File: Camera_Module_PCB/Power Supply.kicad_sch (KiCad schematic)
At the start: 18 parts

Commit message: Made some small additions and notes
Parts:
- gave numbers to parts that had none: 13
- renumbered C1 to C5, TypeCinput to J4, PMIC to U2
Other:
- note added: "To differentiate VDDA and VDD, we can remove the inductor here and slot the inductor in the capacitor array that is present in the main schematic page"
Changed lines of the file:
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@@
 		)
 	)
+	(text "To differentiate VDDA and VDD,\nwe can remove the inductor \nhere and slot the inductor \nin the capacitor array that \nis present in the main \nschematic page\n"
+		(exclude_from_sim no)
+		(at 72.39 142.748 0)
+		(effects
+			(font
+				(size 1.27 1.27)
+			)
+		)
+	)
 	(text "Type C Connector "
 		(exclude_from_sim no)
@@
 		(dnp no)
 		(fields_autoplaced yes)
-		(property "Reference" "D?"
+		(property "Reference" "D4"
 			(at 157.48 77.1524 90)
 			(effects
@@
 		(on_board yes)
 		(dnp no)
-		(property "Reference" "C?"
+		(property "Reference" "C6"
 			(at 267.97 43.1862 0)
 			(effects
@@
 		(dnp no)
 		(fields_autoplaced yes)
-		(property "Reference" "#PWR?"
+		(property "Reference" "#PWR06"
 			(at 97.79 73.66 0)
 			(effects
@@
 		(dnp no)
 		(fields_autoplaced yes)
-		(property "Reference" "#PWR?"
+		(property "Reference" "#PWR04"
 			(at 35.56 24.13 0)
 			(effects
@@
 		(dnp no)
 		(fields_autoplaced yes)
-		(property "Reference" "#PWR?"
+		(property "Reference" "#PWR013"
 			(at 154.94 53.34 0)
 			(effects
@@
 		(dnp no)
 		(fields_autoplaced yes)
-		(property "Reference" "#PWR?"
+		(property "Reference" "#PWR05"
 			(at 85.09 24.13 0)
 			(effects
@@
 		(dnp no)
 		(fields_autoplaced yes)
-		(property "Reference" "#PWR?"
+		(property "Reference" "#PWR017"
 			(at 246.38 95.25 0)
 			(effects
@@
 		(dnp no)
 		(fields_autoplaced yes)
-		(property "Reference" "R?"
+		(property "Reference" "R3"
 			(at 139.7 68.5799 0)
 			(effects
@@
 		(dnp no)
 		(fields_autoplaced yes)
-		(property "Reference" "U?"
+		(property "Reference" "U3"
 			(at 62.23 114.3 0)
 			(effects
@@
 		(dnp no)
 		(fields_autoplaced yes)
-		(property "Reference" "#PWR?"
+		(property "Reference" "#PWR09"
 			(at 100.33 46.99 0)
 			(effects
@@
 		(dnp no)
 		(fields_autoplaced yes)
-		(property "Reference" "TypeCinput"
+		(property "Reference" "J4"
 			(at 60.96 25.4 0)
 			(effects
@@
 		(dnp no)
 		(fields_autoplaced yes)
-		(property "Reference" "R?"
+		(property "Reference" "R4"
 			(at 148.59 68.5799 0)
 			(effects
@@
 		(dnp no)
 		(fields_autoplaced yes)
-		(property "Reference" "PMIC"
+		(property "Reference" "U2"
 			(at 209.55 38.1 0)
 			(effects
@@
 		(dnp no)
 		(fields_autoplaced yes)
-		(property "Reference" "C?"
+		(property "Reference" "C1"
 			(at 123.19 129.5462 0)
 			(effects
@@
 		(dnp no)
 		(fields_autoplaced yes)
-		(property "Reference" "SW?"
+		(property "Reference" "SW2"
 			(at 260.35 81.28 0)
 			(effects
@@
 		(dnp no)
 		(fields_autoplaced yes)
-		(property "Reference" "D?"
+		(property "Reference" "D2"
 			(at 139.7 77.1524 90)
 			(effects
@@
 		(dnp no)
 		(fields_autoplaced yes)
-		(property "Reference" "R?"
+		(property "Reference" "R6"
 			(at 271.78 80.0099 0)
 			(effects
@@
 		(dnp no)
 		(fields_autoplaced yes)
-		(property "Reference" "#PWR?"
+		(property "Reference" "#PWR016"
 			(at 273.05 43.18 0)
 			(effects
@@
 		(dnp no)
 		(fields_autoplaced yes)
-		(property "Reference" "#PWR?"
+		(property "Reference" "#PWR012"
 			(at 119.38 127 0)
 			(effects
@@
 		(dnp no)
 		(fields_autoplaced yes)
-		(property "Reference" "R?"
+		(property "Reference" "R5"
 			(at 157.48 68.5799 0)
 			(effects
@@
 		(on_board yes)
 		(dnp no)
-		(property "Reference" "#PWR?"
+		(property "Reference" "#PWR015"
 			(at 265.43 53.34 0)
 			(effects
@@
 		(dnp no)
 		(fields_autoplaced yes)
-		(property "Reference" "C1"
+		(property "Reference" "C5"
 			(at 102.87 36.8362 0)
 			(effects
@@
 		(on_board yes)
 		(dnp no)
-		(property "Reference" "L?"
+		(property "Reference" "L1"
 			(at 102.87 128.27 0)
 			(effects
@@
 		(dnp no)
 		(fields_autoplaced yes)
-		(property "Reference" "#PWR?"
+		(property "Reference" "#PWR01"
 			(at 120.65 146.05 0)
 			(effects
@@
 		(dnp no)
 		(fields_autoplaced yes)
-		(property "Reference" "#PWR?"
+		(property "Reference" "#PWR08"
 			(at 22.86 52.07 0)
 			(effects
@@
 		(dnp no)
 		(fields_autoplaced yes)
-		(property "Reference" "#PWR?"
+		(property "Reference" "#PWR011"
 			(at 135.89 124.46 0)
 			(effects
@@
 		(dnp no)
 		(fields_autoplaced yes)
-		(property "Reference" "#PWR?"
+		(property "Reference" "#PWR03"
 			(at 25.4 132.08 0)
 			(effects
@@
 		(dnp no)
 		(fields_autoplaced yes)
-		(property "Reference" "#PWR?"
+		(property "Reference" "#PWR07"
 			(at 35.56 71.12 0)
 			(effects
@@
 		(dnp no)
 		(fields_autoplaced yes)
-		(property "Reference" "#PWR?"
+		(property "Reference" "#PWR02"
 			(at 101.6 104.14 0)
 			(effects
@@
 		(dnp no)
 		(fields_autoplaced yes)
-		(property "Reference" "D?"
+		(property "Reference" "D3"
 			(at 148.59 77.1524 90)
 			(effects
@@
 		(dnp no)
 		(fields_autoplaced yes)
-		(property "Reference" "C?"
+		(property "Reference" "C2"
 			(at 104.14 115.5635 0)
 			(effects

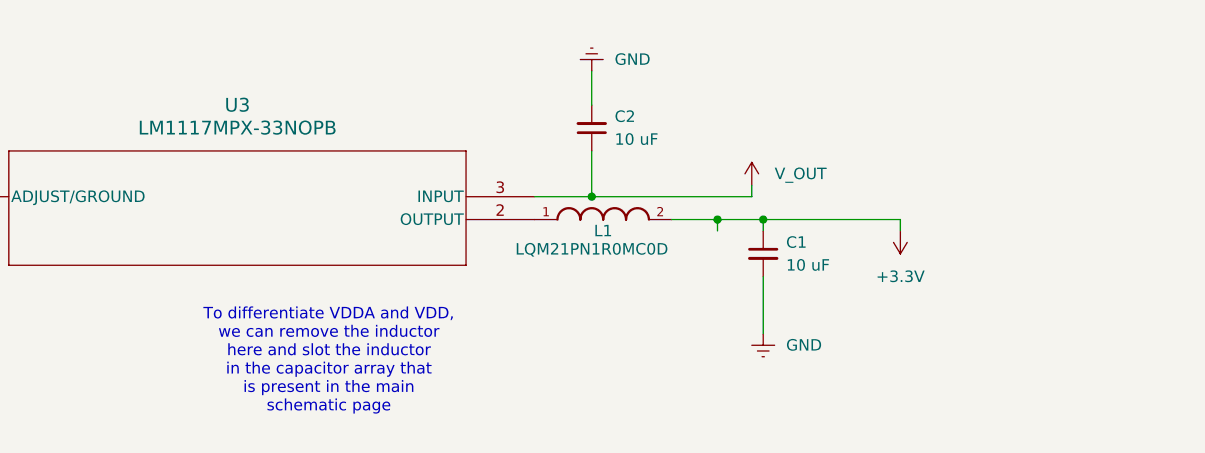
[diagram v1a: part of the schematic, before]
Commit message: Added components and began connections
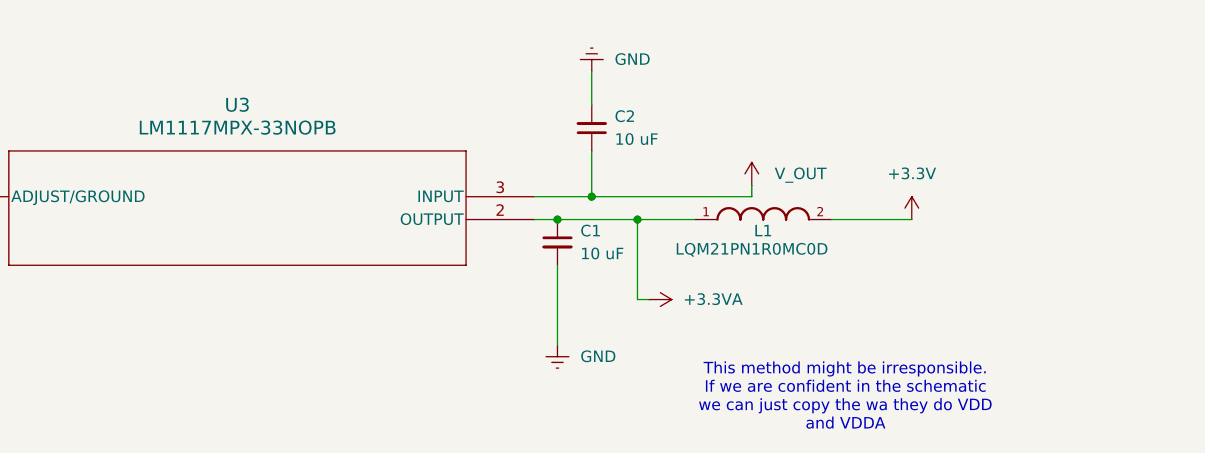
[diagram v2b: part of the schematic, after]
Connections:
- net +3.3V: no longer C1.1
- net +3.3VA: now reaches L1.1, U3.2 (OUTPUT)
- net +3.3VA: now also C1.1
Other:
- note added: "This method might be irresponsible. If we are confident in the schematic we can just copy the wa they do VDD and VDDA"
- note removed: "To differentiate VDDA and VDD, we can remove the inductor here and slot the inductor in the capacitor array that is present in the main schematic page"
- moved on the sheet: C1, L1

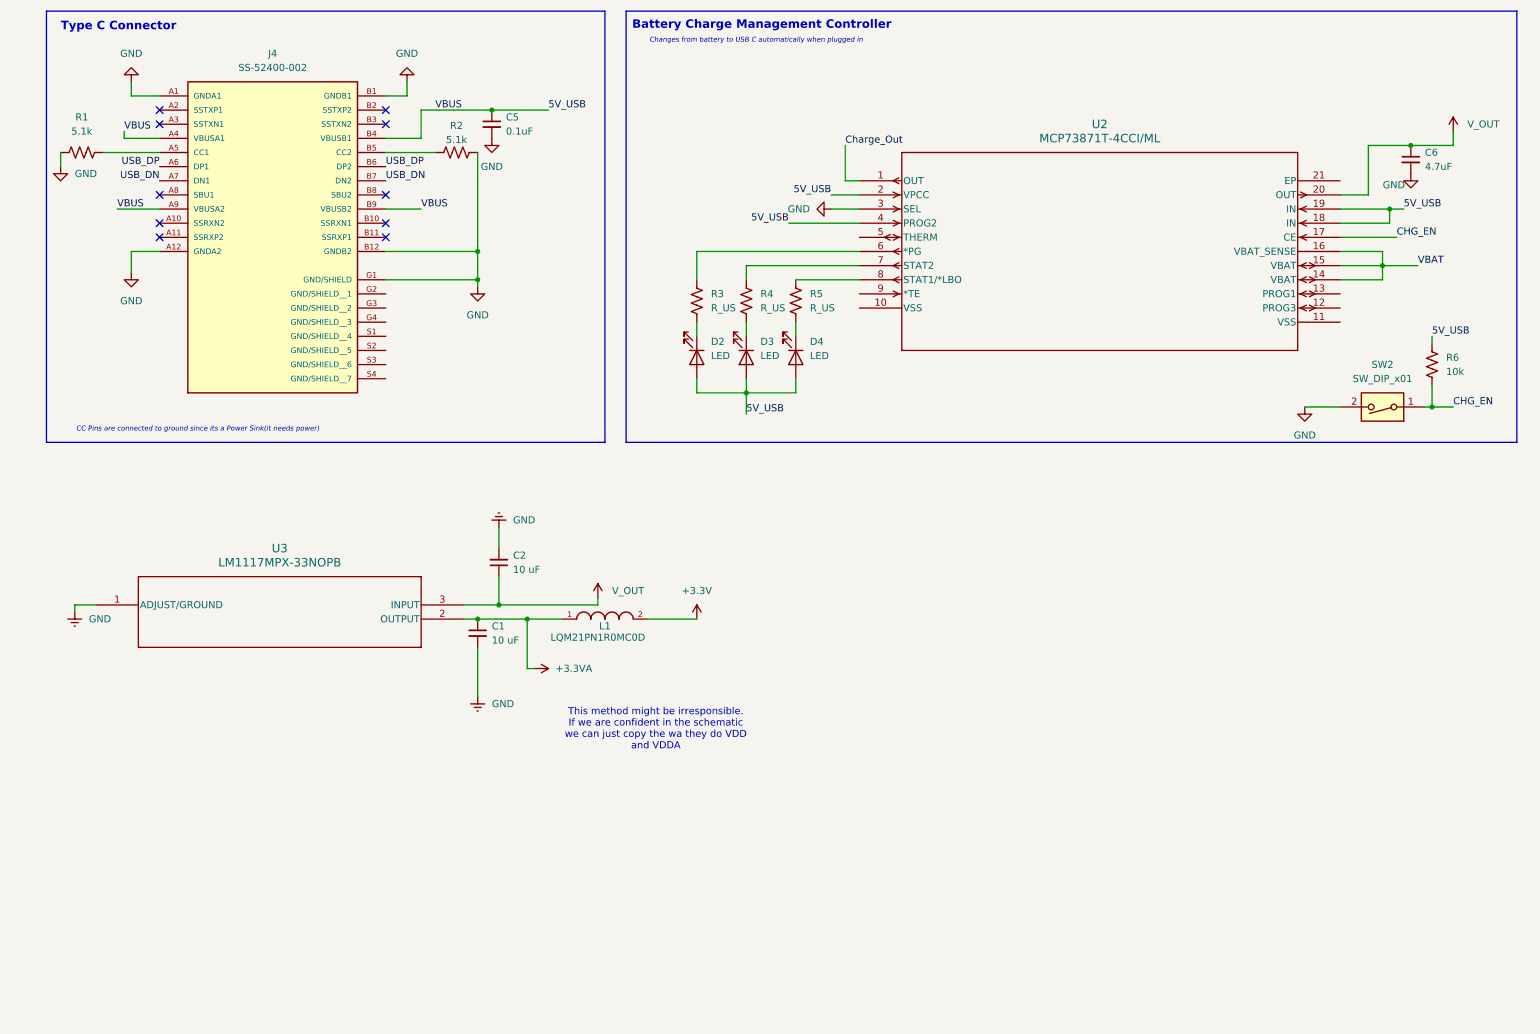
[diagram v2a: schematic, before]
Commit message: ESP32 Modified
-Changed ESP32 to ESP32R8
-Changed ESP32 Filtering
-Can you simulate the VDDA output?
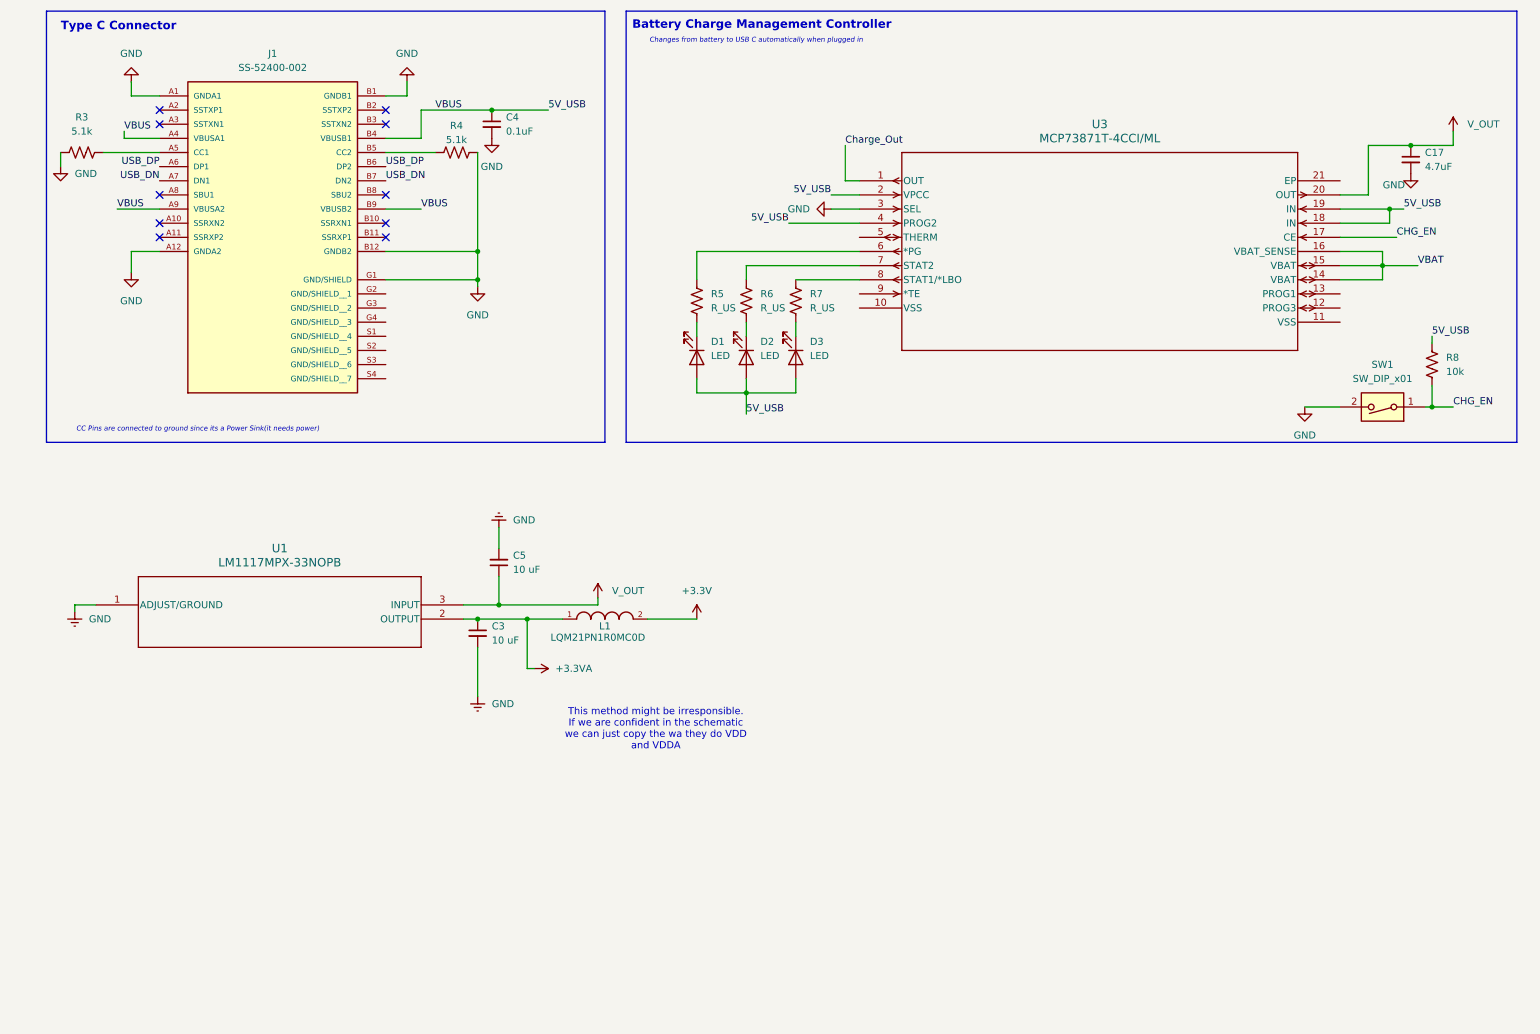
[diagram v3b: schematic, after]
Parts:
- renumbered C6 to C17, C1 to C3, C5 to C4, C2 to C5, D2 to D1, D3 to D2, D4 to D3, J4 to J1, R1 to R3, R2 to R4, R3 to R5, R4 to R6, R5 to R7, R6 to R8, SW2 to SW1, U3 to U1, U2 to U3

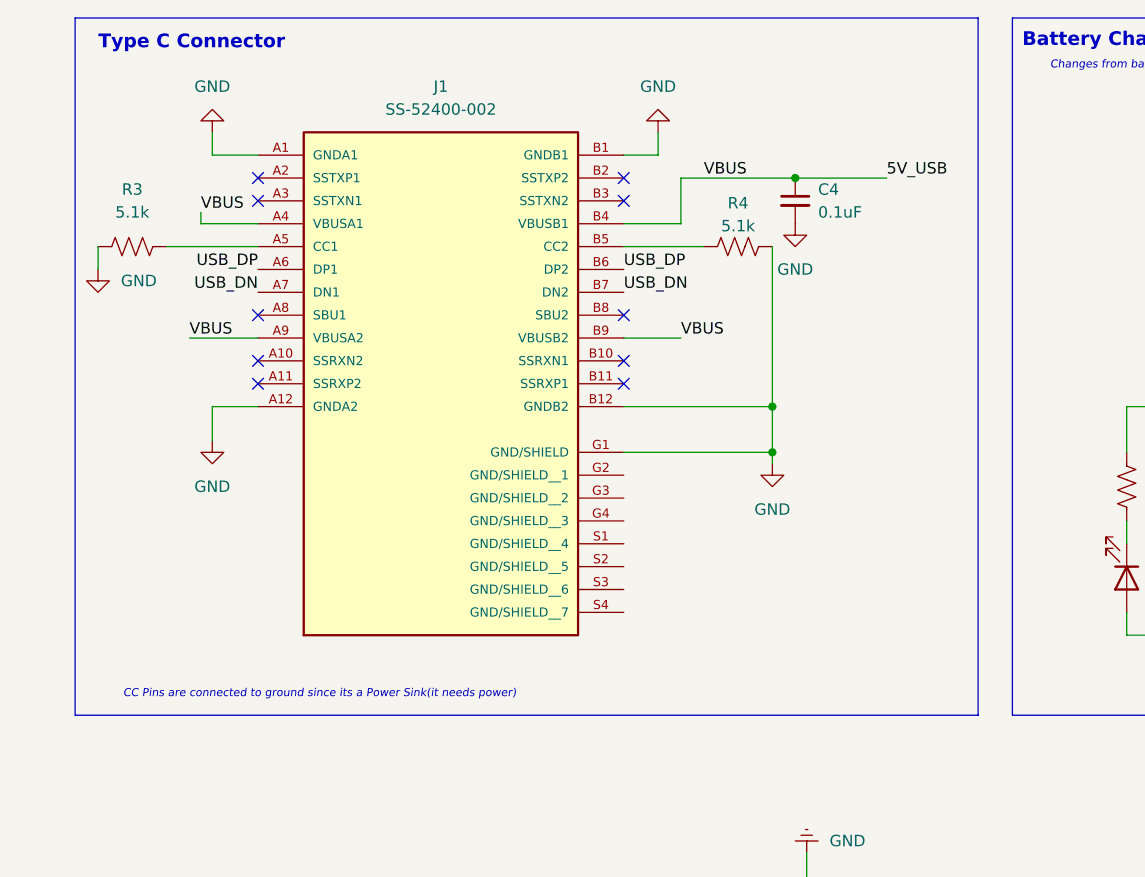
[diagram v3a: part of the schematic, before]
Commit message: Added more minor circuits w/ notes
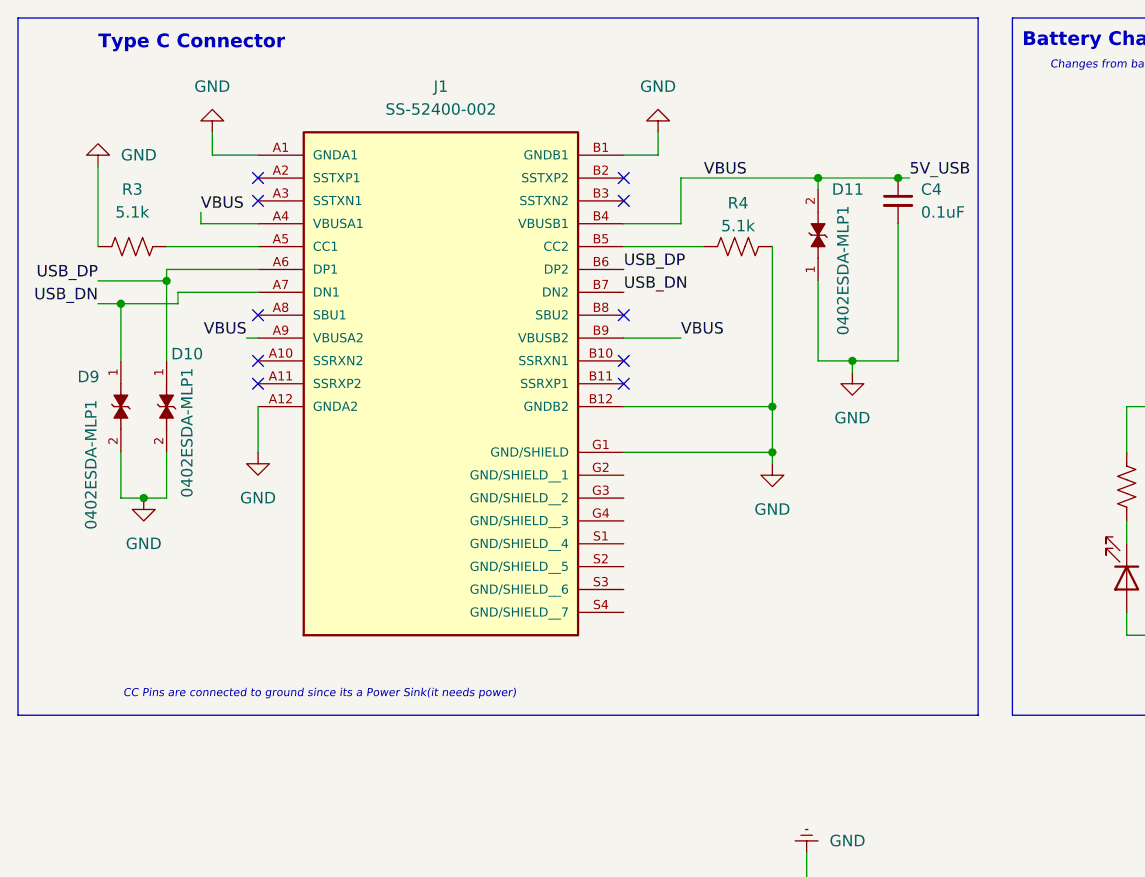
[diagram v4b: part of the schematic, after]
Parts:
- added D10, D11, D9: 0402ESDA-MLP1, 0402ESDA-MLP1:ESD_0402ESDA-MLP1, symbol 0402ESDA-MLP1:0402ESDA-MLP1
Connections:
- net 5V_USB: now also D11.2
- net GND: now also D10.2, D11.1, D9.2
- net USB_DN: now also D9.1
- net USB_DP: now also D10.1
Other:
- moved on the sheet: C4

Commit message: Made connections to FPC Connector
I connected the MCU pins to the FPC connector for the camera module. There is still power missing for the FPC connector for 2.8V and 1.5V. We still need to wire some pins to ESD protection ICs, should be easy.
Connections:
- net USB_DN renamed USB_D-
- net USB_DP renamed USB_D+
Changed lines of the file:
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@@
 		)
 	)
-	(label "USB_DP"
+	(label "USB_D+"
 		(at 22.86 46.99 180)
 		(effects
@@
 		)
 	)
-	(label "USB_DN"
+	(label "USB_D-"
 		(at 81.28 48.26 0)
 		(effects
@@
 		)
 	)
-	(label "USB_DN"
+	(label "USB_D-"
 		(at 22.86 49.53 180)
 		(effects
@@
 		)
 	)
-	(label "USB_DP"
+	(label "USB_D+"
 		(at 81.28 45.72 0)
 		(effects

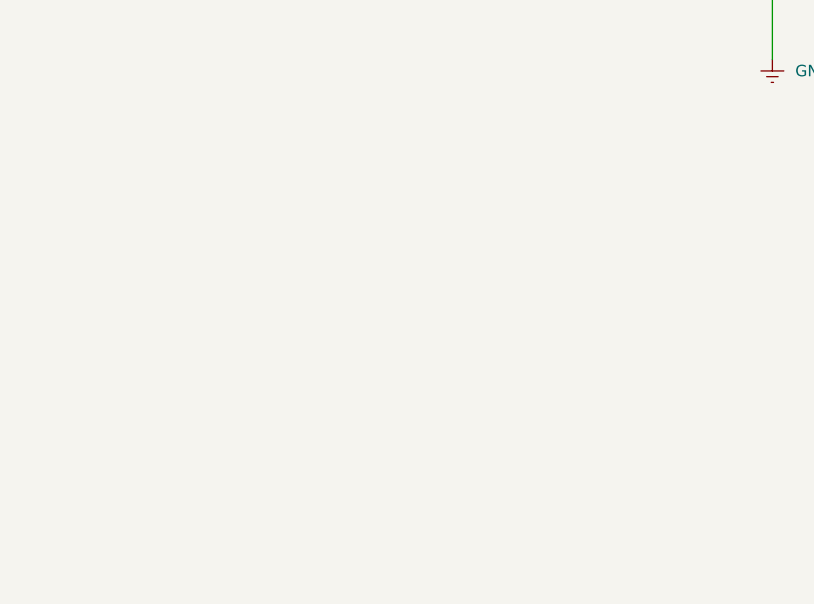
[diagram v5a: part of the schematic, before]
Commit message: Added most of the remaining components
Added the microphone, two LDO regulators, light sensor, and LED driver. The missing components will be passive elements and specific infared LEDs for the LED driver.
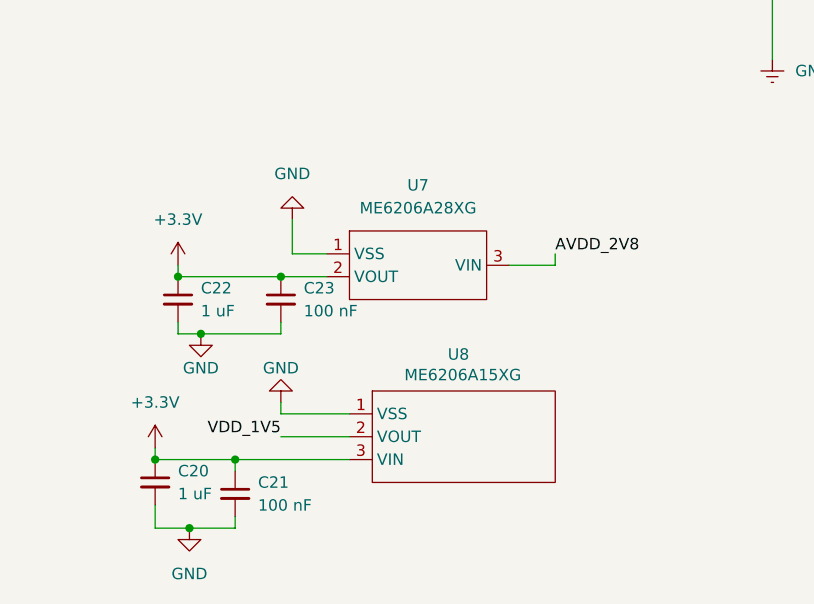
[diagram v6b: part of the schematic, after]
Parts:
- added C20, C22: 1 uF, symbol Device:C_Small
- added C21, C23: 100 nF, symbol Device:C_Small
- added U7: ME6206A28XG, ME6206A28XG:SOT-23_L2.9-W1.3-P1.90-LS2.4-BR, symbol ME6206A28XG:ME6206A28XG
- added U8: ME6206A15XG, ME6206A15XG:SOT-23-3_L2.9-W1.6-P1.90-LS2.8-BR, symbol ME6206A15XG:ME6206A15XG
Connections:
- net +3.3V: now also C20.1, C21.1, C22.1, C23.1, U7.2 (VOUT), U8.3 (VIN)
- net GND: now also C20.2, C21.2, C22.2, C23.2, U7.1 (VSS), U8.1 (VSS)
- new net AVDD_2V8: U7.3 (VIN)
- new net VDD_1V5: U8.2 (VOUT)

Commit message: Minor Changes
Minor Chanhes
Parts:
- renumbered U8 to 1V5_R, U1 to 3V3_R, U7 to 3V8_R, U3 to Battery_Management
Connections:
- net V_OUT renamed V_OUT_BM
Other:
- note added: "Voltage Regulator"
- note removed: "This method might be irresponsible. If we are confident in the schematic we can just copy the wa they do VDD and VDDA"
- moved on the sheet: 1V5_R, 3V3_R, 3V8_R, C20, C21, C22, C23, C3, C5, L1
